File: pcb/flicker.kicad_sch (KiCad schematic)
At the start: 4 parts, among them Q1 SFH300, U1 Pico, U2 AD5220

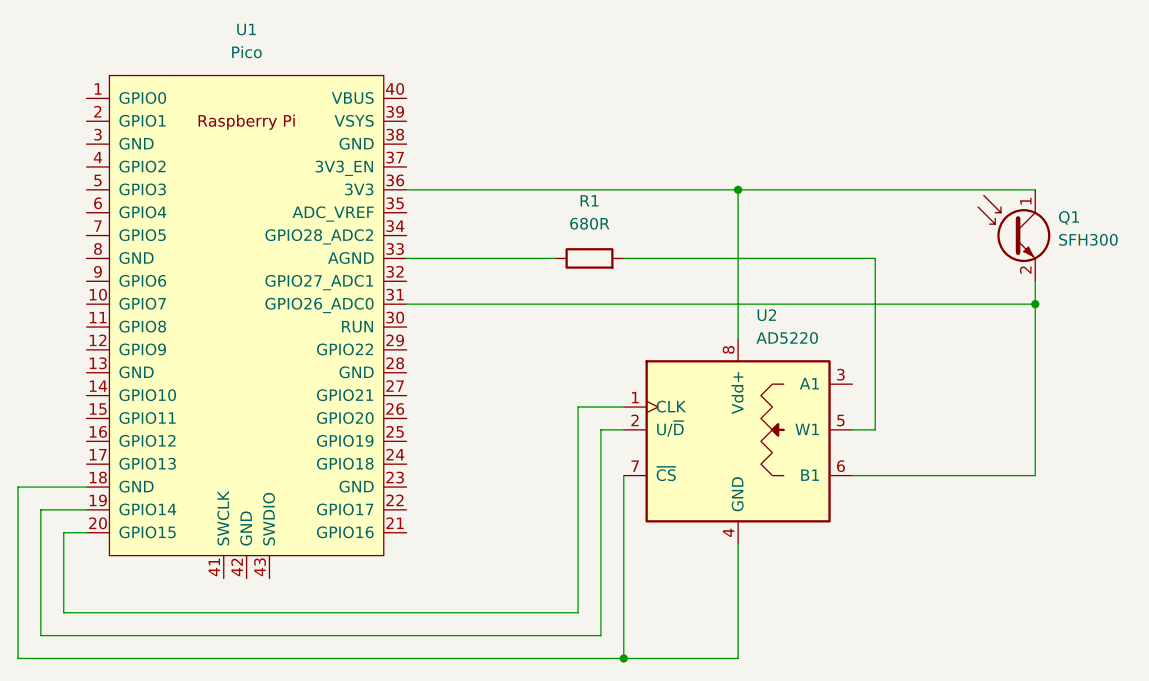
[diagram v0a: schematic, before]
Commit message: PCB: use complete part number for AD5220BNZ10
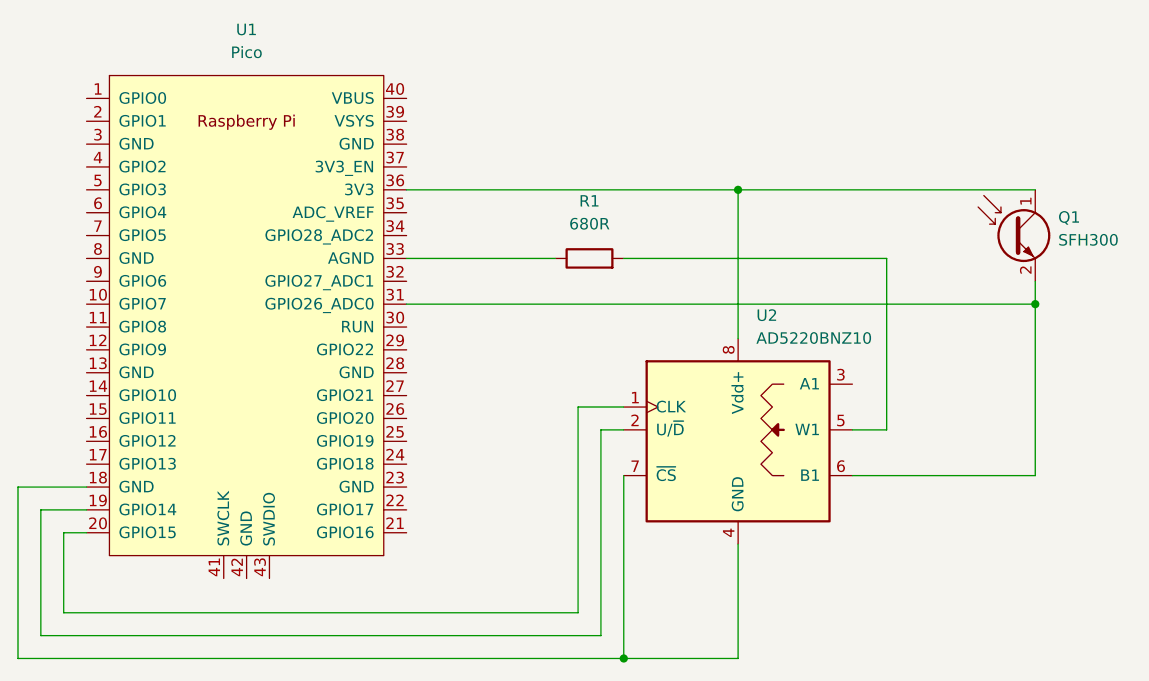
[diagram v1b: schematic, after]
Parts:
- U2: value AD5220 -> AD5220BNZ10
